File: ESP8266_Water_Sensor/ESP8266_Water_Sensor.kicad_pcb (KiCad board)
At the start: 4 copper layers, 54.1 x 54.1 mm, 38 parts, among them J1 Conn_01x06_Female, J2 691137710002, J3 691137710003, J4 691137710002, J5 Conn_01x06_Female, U1 ESP-WROOM-02D_M1102H3200PH3Q0_, U2 AP6502SP-13

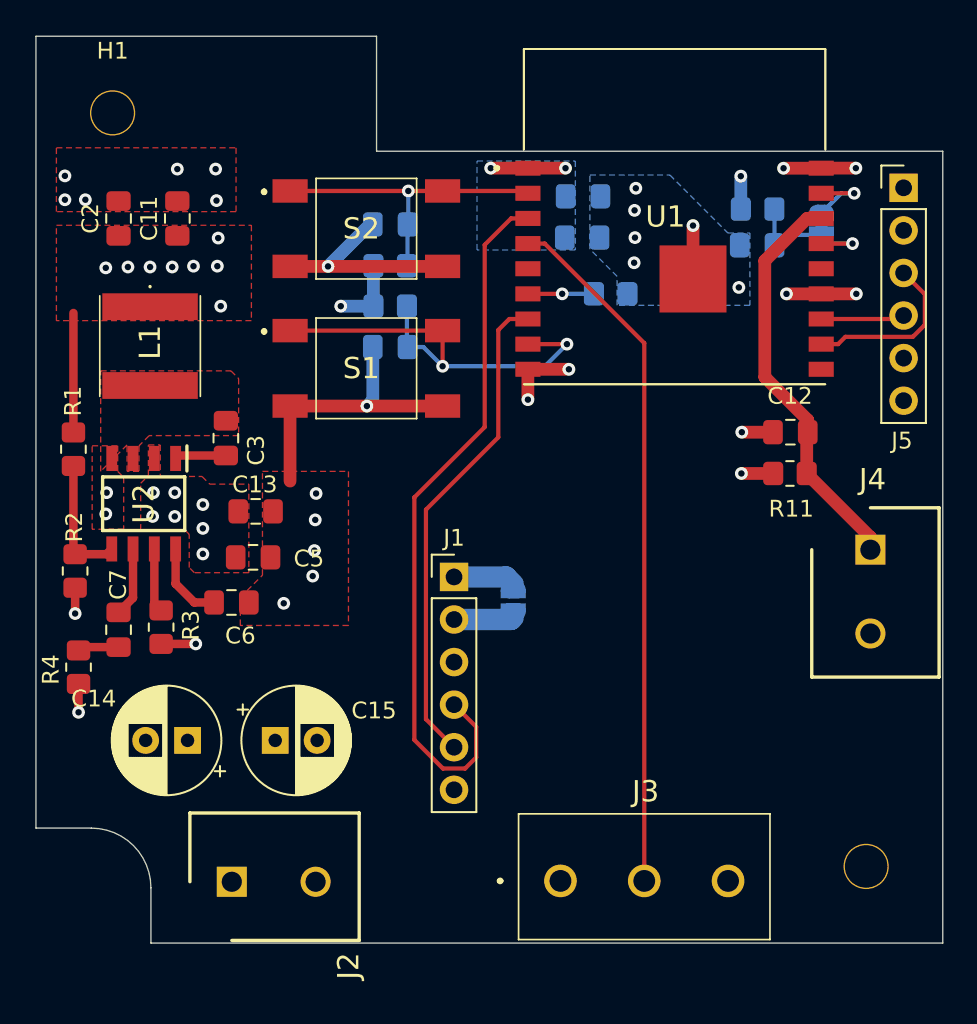
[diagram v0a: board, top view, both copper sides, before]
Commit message: edited the silkscreen
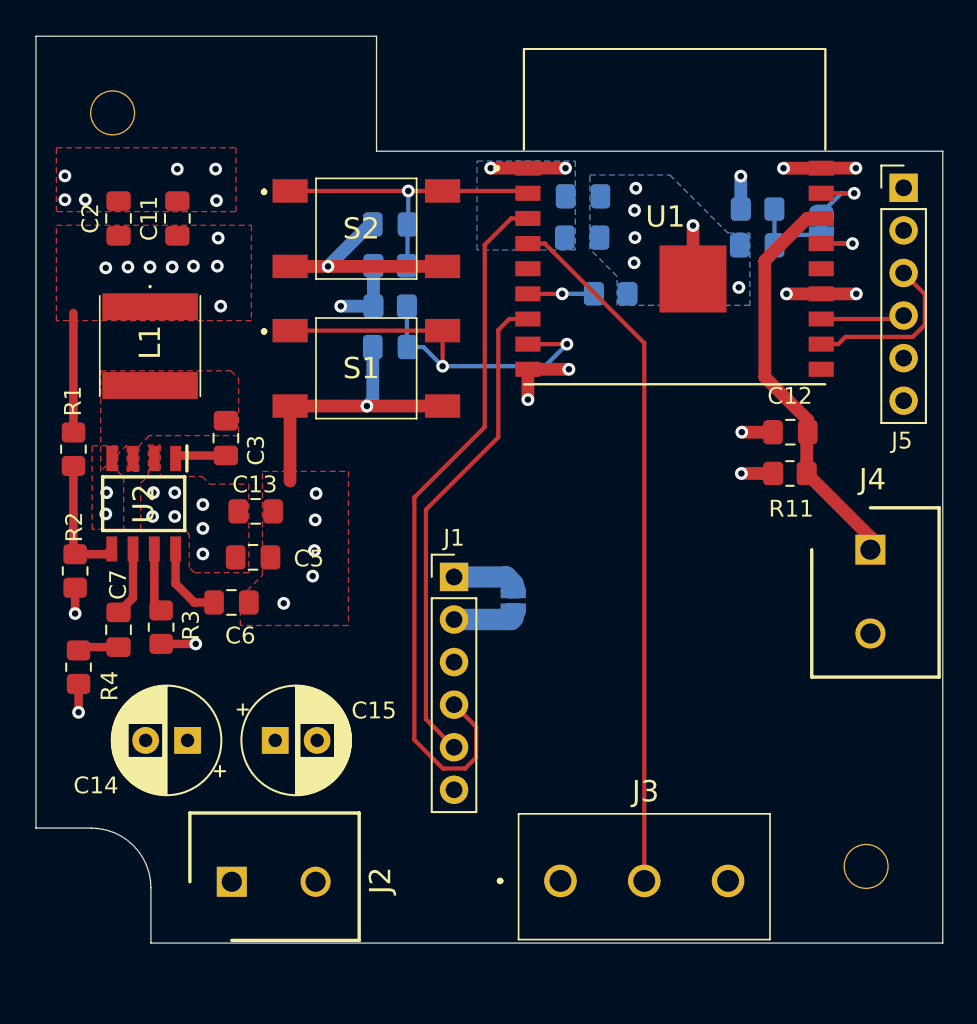
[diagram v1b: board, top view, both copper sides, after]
